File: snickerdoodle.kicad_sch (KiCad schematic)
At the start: 8 parts, among them P2 TFM-115-01-F-D-A, P3 TFM-120-01-F-D-A

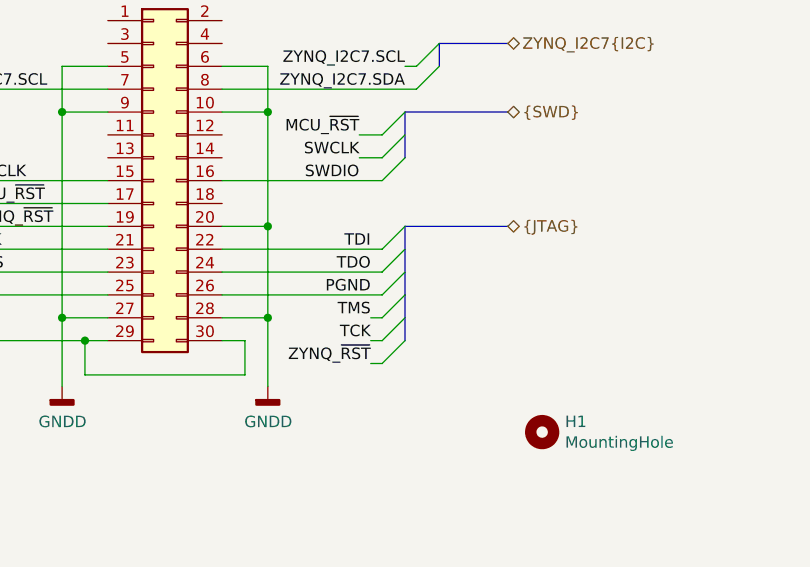
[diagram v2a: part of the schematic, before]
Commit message: Working on gigabit ethernet PHY
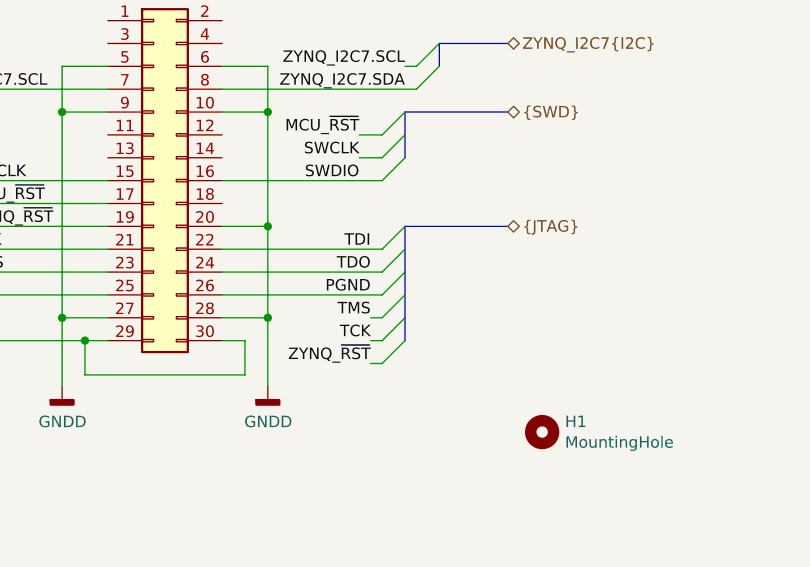
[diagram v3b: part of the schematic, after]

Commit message: Annotate schematic
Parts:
- renumbered H1 to H401, P2 to P401, P3 to P402, PA1 to PA401, PA2 to PA402, PB1 to PB401, PB2 to PB402, PC1 to PC401
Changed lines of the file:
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@@
-(kicad_sch (version 20200618) (host eeschema "5.99.0-unknown-1463dd1~101~ubuntu20.04.1")
-  (page 4 13)
-  (paper "A4")
+(kicad_sch (version 20200618) (host eeschema "5.99.0-unknown-77313e4~101~ubuntu20.04.1")
+  (page 1 13)
+  (paper "B")
   (title_block
     (title "Snickerdoodle Interconnect")
@@
     (comment 1 "Drawn by: Cameron McQuinn")
   )
+  (bus_alias "INTERRUPT" (members "~INT1" "~INT2"))
+  (bus_alias "I2C" (members "SDA" "SCL"))
+  (bus_alias "JTAG" (members "TDI" "TDO" "TCK" "TMS" "ZYNQ_~RST" "PGND"))
   (bus_alias "SWD" (members "MCU_~RST" "SWCLK" "SWDIO"))
-  (bus_alias "JTAG" (members "TDI" "TDO" "TCK" "TMS" "ZYNQ_~RST" "PGND"))
-  (bus_alias "I2C" (members "SDA" "SCL"))
-  (bus_alias "INTERRUPT" (members "~INT1" "~INT2"))
   (junction (at 40.64 45.72) (diameter 0) (color 0 0 0 0))
   (junction (at 40.64 53.34) (diameter 0) (color 0 0 0 0))
@@
   (symbol (lib_id "Snickerdoodle:3.3V_VIO") (at 182.88 134.62 0) (unit 1)
     (in_bom yes) (on_board yes)
-    (property "Reference" "#PWR0115" (id 0) (at 182.88 138.43 0)
+    (property "Reference" "#PWR0410" (id 0) (at 182.88 138.43 0)
       (effects (font (size 1.27 1.27)) hide)
     )
@@
   (symbol (lib_id "power:GNDD") (at 40.64 83.82 0) (mirror y) (unit 1)
     (in_bom yes) (on_board yes)
-    (property "Reference" "#PWR0106" (id 0) (at 40.64 90.17 0)
+    (property "Reference" "#PWR0401" (id 0) (at 40.64 90.17 0)
       (effects (font (size 1.27 1.27)) hide)
     )
@@
   (symbol (lib_id "power:GNDD") (at 40.64 185.42 0) (mirror y) (unit 1)
     (in_bom yes) (on_board yes)
-    (property "Reference" "#PWR0108" (id 0) (at 40.64 191.77 0)
+    (property "Reference" "#PWR0402" (id 0) (at 40.64 191.77 0)
       (effects (font (size 1.27 1.27)) hide)
     )
@@
   (symbol (lib_id "power:GNDD") (at 63.5 83.82 0) (unit 1)
     (in_bom yes) (on_board yes)
-    (property "Reference" "#PWR0104" (id 0) (at 63.5 90.17 0)
+    (property "Reference" "#PWR0403" (id 0) (at 63.5 90.17 0)
       (effects (font (size 1.27 1.27)) hide)
     )
@@
   (symbol (lib_id "power:GNDD") (at 63.5 185.42 0) (unit 1)
     (in_bom yes) (on_board yes)
-    (property "Reference" "#PWR0107" (id 0) (at 63.5 191.77 0)
+    (property "Reference" "#PWR0404" (id 0) (at 63.5 191.77 0)
       (effects (font (size 1.27 1.27)) hide)
     )
@@
   (symbol (lib_id "power:GNDD") (at 104.14 83.82 0) (mirror y) (unit 1)
     (in_bom yes) (on_board yes)
-    (property "Reference" "#PWR0105" (id 0) (at 104.14 90.17 0)
+    (property "Reference" "#PWR0405" (id 0) (at 104.14 90.17 0)
       (effects (font (size 1.27 1.27)) hide)
     )
@@
   (symbol (lib_id "power:GNDD") (at 104.14 185.42 0) (mirror y) (unit 1)
     (in_bom yes) (on_board yes)
-    (property "Reference" "#PWR0101" (id 0) (at 104.14 191.77 0)
+    (property "Reference" "#PWR0406" (id 0) (at 104.14 191.77 0)
       (effects (font (size 1.27 1.27)) hide)
     )
@@
   (symbol (lib_id "power:GNDD") (at 127 83.82 0) (unit 1)
     (in_bom yes) (on_board yes)
-    (property "Reference" "#PWR0103" (id 0) (at 127 90.17 0)
+    (property "Reference" "#PWR0407" (id 0) (at 127 90.17 0)
       (effects (font (size 1.27 1.27)) hide)
     )
@@
   (symbol (lib_id "power:GNDD") (at 127 185.42 0) (unit 1)
     (in_bom yes) (on_board yes)
-    (property "Reference" "#PWR0102" (id 0) (at 127 191.77 0)
+    (property "Reference" "#PWR0408" (id 0) (at 127 191.77 0)
       (effects (font (size 1.27 1.27)) hide)
     )
@@
   (symbol (lib_id "power:GNDD") (at 167.64 83.82 0) (mirror y) (unit 1)
     (in_bom yes) (on_board yes)
-    (property "Reference" "#PWR0113" (id 0) (at 167.64 90.17 0)
+    (property "Reference" "#PWR0409" (id 0) (at 167.64 90.17 0)
       (effects (font (size 1.27 1.27)) hide)
     )
@@
   (symbol (lib_id "power:GNDD") (at 190.5 83.82 0) (unit 1)
     (in_bom yes) (on_board yes)
-    (property "Reference" "#PWR0114" (id 0) (at 190.5 90.17 0)
+    (property "Reference" "#PWR0411" (id 0) (at 190.5 90.17 0)
       (effects (font (size 1.27 1.27)) hide)
     )
@@
   (symbol (lib_id "power:GNDD") (at 200.66 147.32 0) (unit 1)
     (in_bom yes) (on_board yes)
-    (property "Reference" "#PWR0109" (id 0) (at 200.66 153.67 0)
+    (property "Reference" "#PWR0412" (id 0) (at 200.66 153.67 0)
       (effects (font (size 1.27 1.27)) hide)
     )
@@
   (symbol (lib_id "power:GNDD") (at 223.52 147.32 0) (unit 1)
     (in_bom yes) (on_board yes)
-    (property "Reference" "#PWR0112" (id 0) (at 223.52 153.67 0)
+    (property "Reference" "#PWR0413" (id 0) (at 223.52 153.67 0)
       (effects (font (size 1.27 1.27)) hide)
     )
@@
   (symbol (lib_id "power:GNDD") (at 231.14 83.82 0) (mirror y) (unit 1)
     (in_bom yes) (on_board yes)
-    (property "Reference" "#PWR0110" (id 0) (at 231.14 90.17 0)
+    (property "Reference" "#PWR0414" (id 0) (at 231.14 90.17 0)
       (effects (font (size 1.27 1.27)) hide)
     )
@@
   (symbol (lib_id "power:GNDD") (at 254 83.82 0) (unit 1)
     (in_bom yes) (on_board yes)
-    (property "Reference" "#PWR0111" (id 0) (at 254 90.17 0)
+    (property "Reference" "#PWR0415" (id 0) (at 254 90.17 0)
       (effects (font (size 1.27 1.27)) hide)
     )
@@
   (symbol (lib_id "Mechanical:MountingHole") (at 254 152.4 0) (unit 1)
     (in_bom yes) (on_board yes)
-    (property "Reference" "H1" (id 0) (at 256.5401 151.2506 0)
+    (property "Reference" "H401" (id 0) (at 256.5401 151.2506 0)
       (effects (font (size 1.27 1.27)) (justify left))
     )
@@
   (symbol (lib_id "Connector_Generic:Conn_02x15_Odd_Even") (at 210.82 124.46 0) (unit 1)
     (in_bom yes) (on_board yes)
-    (property "Reference" "P2" (id 0) (at 212.09 101.1998 0))
+    (property "Reference" "P401" (id 0) (at 212.09 101.1998 0))
     (property "Value" "TFM-115-01-F-D-A" (id 1) (at 212.09 103.4985 0))
     (property "Footprint" "Connector_Samtec_TFM:Samtec_TFM-115-01-F-D-A_2x15_P1.27mm_Horizontal" (id 2) (at 210.82 124.46 0)
@@
   (symbol (lib_id "Connector_Generic:Conn_02x20_Odd_Even") (at 50.8 50.8 0) (unit 1)
     (in_bom yes) (on_board yes)
-    (property "Reference" "PA1" (id 0) (at 52.07 22.46 0))
+    (property "Reference" "PA401" (id 0) (at 52.07 22.46 0))
     (property "Value" "TFM-120-01-F-D-A" (id 1) (at 52.07 24.7585 0))
     (property "Footprint" "Connector_Samtec_TFM:Samtec_TFM-120-01-F-D-A_2x20_P1.27mm_Horizontal" (id 2) (at 50.8 50.8 0)
@@
   (symbol (lib_id "Connector_Generic:Conn_02x20_Odd_Even") (at 50.8 152.4 0) (unit 1)
     (in_bom yes) (on_board yes)
-    (property "Reference" "PB1" (id 0) (at 52.07 124.06 0))
+    (property "Reference" "PB401" (id 0) (at 52.07 124.06 0))
     (property "Value" "TFM-120-01-F-D-A" (id 1) (at 52.07 126.3585 0))
     (property "Footprint" "Connector_Samtec_TFM:Samtec_TFM-120-01-F-D-A_2x20_P1.27mm_Horizontal" (id 2) (at 50.8 152.4 0)
@@
   (symbol (lib_id "Connector_Generic:Conn_02x20_Odd_Even") (at 114.3 50.8 0) (unit 1)
     (in_bom yes) (on_board yes)
-    (property "Reference" "PA2" (id 0) (at 115.57 22.46 0))
+    (property "Reference" "PA402" (id 0) (at 115.57 22.46 0))
     (property "Value" "TFM-120-01-F-D-A" (id 1) (at 115.57 24.7585 0))
     (property "Footprint" "Connector_Samtec_TFM:Samtec_TFM-120-01-F-D-A_2x20_P1.27mm_Horizontal" (id 2) (at 114.3 50.8 0)
@@
   (symbol (lib_id "Connector_Generic:Conn_02x20_Odd_Even") (at 114.3 152.4 0) (unit 1)
     (in_bom yes) (on_board yes)
-    (property "Reference" "PB2" (id 0) (at 115.57 124.06 0))
+    (property "Reference" "PB402" (id 0) (at 115.57 124.06 0))
     (property "Value" "TFM-120-01-F-D-A" (id 1) (at 115.57 126.3585 0))
     (property "Footprint" "Connector_Samtec_TFM:Samtec_TFM-120-01-F-D-A_2x20_P1.27mm_Horizontal" (id 2) (at 114.3 152.4 0)
@@
   (symbol (lib_id "Connector_Generic:Conn_02x20_Odd_Even") (at 177.8 50.8 0) (unit 1)
     (in_bom yes) (on_board yes)
-    (property "Reference" "PC1" (id 0) (at 179.07 22.46 0))
+    (property "Reference" "PC401" (id 0) (at 179.07 22.46 0))
     (property "Value" "TFM-120-01-F-D-A" (id 1) (at 179.07 24.7585 0))
     (property "Footprint" "Connector_Samtec_TFM:Samtec_TFM-120-01-F-D-A_2x20_P1.27mm_Horizontal" (id 2) (at 177.8 50.8 0)
@@
   (symbol (lib_id "Connector_Generic:Conn_02x20_Odd_Even") (at 241.3 50.8 0) (unit 1)
     (in_bom yes) (on_board yes)
-    (property "Reference" "P3" (id 0) (at 242.57 22.46 0))
+    (property "Reference" "P402" (id 0) (at 242.57 22.46 0))
     (property "Value" "TFM-120-01-F-D-A" (id 1) (at 242.57 24.7585 0))
     (property "Footprint" "Connector_Samtec_TFM:Samtec_TFM-120-01-F-D-A_2x20_P1.27mm_Horizontal" (id 2) (at 241.3 50.8 0)

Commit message: Fix footprint associations, use 74LVC2G07 instead of MOSFETs
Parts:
- renumbered H401 to H501, P401 to P501, P402 to P502, PA401 to PA501, PA402 to PA502, PB401 to PB501, PB402 to PB502, PC401 to PC501
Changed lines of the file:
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@@
     (comment 1 "Drawn by: Cameron McQuinn")
   )
-  (bus_alias "INTERRUPT" (members "~INT1" "~INT2"))
+  (bus_alias "SWD" (members "MCU_~RST" "SWCLK" "SWDIO"))
   (bus_alias "I2C" (members "SDA" "SCL"))
   (bus_alias "JTAG" (members "TDI" "TDO" "TCK" "TMS" "ZYNQ_~RST" "PGND"))
-  (bus_alias "SWD" (members "MCU_~RST" "SWCLK" "SWDIO"))
+  (bus_alias "INTERRUPT" (members "~INT1" "~INT2"))
   (junction (at 40.64 45.72) (diameter 0) (color 0 0 0 0))
   (junction (at 40.64 53.34) (diameter 0) (color 0 0 0 0))
@@
   (symbol (lib_id "Snickerdoodle:3.3V_VIO") (at 182.88 134.62 0) (unit 1)
     (in_bom yes) (on_board yes)
-    (property "Reference" "#PWR0410" (id 0) (at 182.88 138.43 0)
+    (property "Reference" "#PWR0510" (id 0) (at 182.88 138.43 0)
       (effects (font (size 1.27 1.27)) hide)
     )
@@
   (symbol (lib_id "power:GNDD") (at 40.64 83.82 0) (mirror y) (unit 1)
     (in_bom yes) (on_board yes)
-    (property "Reference" "#PWR0401" (id 0) (at 40.64 90.17 0)
+    (property "Reference" "#PWR0501" (id 0) (at 40.64 90.17 0)
       (effects (font (size 1.27 1.27)) hide)
     )
@@
   (symbol (lib_id "power:GNDD") (at 40.64 185.42 0) (mirror y) (unit 1)
     (in_bom yes) (on_board yes)
-    (property "Reference" "#PWR0402" (id 0) (at 40.64 191.77 0)
+    (property "Reference" "#PWR0502" (id 0) (at 40.64 191.77 0)
       (effects (font (size 1.27 1.27)) hide)
     )
@@
   (symbol (lib_id "power:GNDD") (at 63.5 83.82 0) (unit 1)
     (in_bom yes) (on_board yes)
-    (property "Reference" "#PWR0403" (id 0) (at 63.5 90.17 0)
+    (property "Reference" "#PWR0503" (id 0) (at 63.5 90.17 0)
       (effects (font (size 1.27 1.27)) hide)
     )
@@
   (symbol (lib_id "power:GNDD") (at 63.5 185.42 0) (unit 1)
     (in_bom yes) (on_board yes)
-    (property "Reference" "#PWR0404" (id 0) (at 63.5 191.77 0)
+    (property "Reference" "#PWR0504" (id 0) (at 63.5 191.77 0)
       (effects (font (size 1.27 1.27)) hide)
     )
@@
   (symbol (lib_id "power:GNDD") (at 104.14 83.82 0) (mirror y) (unit 1)
     (in_bom yes) (on_board yes)
-    (property "Reference" "#PWR0405" (id 0) (at 104.14 90.17 0)
+    (property "Reference" "#PWR0505" (id 0) (at 104.14 90.17 0)
       (effects (font (size 1.27 1.27)) hide)
     )
@@
   (symbol (lib_id "power:GNDD") (at 104.14 185.42 0) (mirror y) (unit 1)
     (in_bom yes) (on_board yes)
-    (property "Reference" "#PWR0406" (id 0) (at 104.14 191.77 0)
+    (property "Reference" "#PWR0506" (id 0) (at 104.14 191.77 0)
       (effects (font (size 1.27 1.27)) hide)
     )
@@
   (symbol (lib_id "power:GNDD") (at 127 83.82 0) (unit 1)
     (in_bom yes) (on_board yes)
-    (property "Reference" "#PWR0407" (id 0) (at 127 90.17 0)
+    (property "Reference" "#PWR0507" (id 0) (at 127 90.17 0)
       (effects (font (size 1.27 1.27)) hide)
     )
@@
   (symbol (lib_id "power:GNDD") (at 127 185.42 0) (unit 1)
     (in_bom yes) (on_board yes)
-    (property "Reference" "#PWR0408" (id 0) (at 127 191.77 0)
+    (property "Reference" "#PWR0508" (id 0) (at 127 191.77 0)
       (effects (font (size 1.27 1.27)) hide)
     )
@@
   (symbol (lib_id "power:GNDD") (at 167.64 83.82 0) (mirror y) (unit 1)
     (in_bom yes) (on_board yes)
-    (property "Reference" "#PWR0409" (id 0) (at 167.64 90.17 0)
+    (property "Reference" "#PWR0509" (id 0) (at 167.64 90.17 0)
       (effects (font (size 1.27 1.27)) hide)
     )
@@
   (symbol (lib_id "power:GNDD") (at 190.5 83.82 0) (unit 1)
     (in_bom yes) (on_board yes)
-    (property "Reference" "#PWR0411" (id 0) (at 190.5 90.17 0)
+    (property "Reference" "#PWR0511" (id 0) (at 190.5 90.17 0)
       (effects (font (size 1.27 1.27)) hide)
     )
@@
   (symbol (lib_id "power:GNDD") (at 200.66 147.32 0) (unit 1)
     (in_bom yes) (on_board yes)
-    (property "Reference" "#PWR0412" (id 0) (at 200.66 153.67 0)
+    (property "Reference" "#PWR0512" (id 0) (at 200.66 153.67 0)
       (effects (font (size 1.27 1.27)) hide)
     )
@@
   (symbol (lib_id "power:GNDD") (at 223.52 147.32 0) (unit 1)
     (in_bom yes) (on_board yes)
-    (property "Reference" "#PWR0413" (id 0) (at 223.52 153.67 0)
+    (property "Reference" "#PWR0513" (id 0) (at 223.52 153.67 0)
       (effects (font (size 1.27 1.27)) hide)
     )
@@
   (symbol (lib_id "power:GNDD") (at 231.14 83.82 0) (mirror y) (unit 1)
     (in_bom yes) (on_board yes)
-    (property "Reference" "#PWR0414" (id 0) (at 231.14 90.17 0)
+    (property "Reference" "#PWR0514" (id 0) (at 231.14 90.17 0)
       (effects (font (size 1.27 1.27)) hide)
     )
@@
   (symbol (lib_id "power:GNDD") (at 254 83.82 0) (unit 1)
     (in_bom yes) (on_board yes)
-    (property "Reference" "#PWR0415" (id 0) (at 254 90.17 0)
+    (property "Reference" "#PWR0515" (id 0) (at 254 90.17 0)
       (effects (font (size 1.27 1.27)) hide)
     )
@@
   (symbol (lib_id "Mechanical:MountingHole") (at 254 152.4 0) (unit 1)
     (in_bom yes) (on_board yes)
-    (property "Reference" "H401" (id 0) (at 256.5401 151.2506 0)
+    (property "Reference" "H501" (id 0) (at 256.5401 151.2506 0)
       (effects (font (size 1.27 1.27)) (justify left))
     )
@@
   (symbol (lib_id "Connector_Generic:Conn_02x15_Odd_Even") (at 210.82 124.46 0) (unit 1)
     (in_bom yes) (on_board yes)
-    (property "Reference" "P401" (id 0) (at 212.09 101.1998 0))
+    (property "Reference" "P501" (id 0) (at 212.09 101.1998 0))
     (property "Value" "TFM-115-01-F-D-A" (id 1) (at 212.09 103.4985 0))
     (property "Footprint" "Connector_Samtec_TFM:Samtec_TFM-115-01-F-D-A_2x15_P1.27mm_Horizontal" (id 2) (at 210.82 124.46 0)
@@
   (symbol (lib_id "Connector_Generic:Conn_02x20_Odd_Even") (at 50.8 50.8 0) (unit 1)
     (in_bom yes) (on_board yes)
-    (property "Reference" "PA401" (id 0) (at 52.07 22.46 0))
+    (property "Reference" "PA501" (id 0) (at 52.07 22.46 0))
     (property "Value" "TFM-120-01-F-D-A" (id 1) (at 52.07 24.7585 0))
     (property "Footprint" "Connector_Samtec_TFM:Samtec_TFM-120-01-F-D-A_2x20_P1.27mm_Horizontal" (id 2) (at 50.8 50.8 0)
@@
   (symbol (lib_id "Connector_Generic:Conn_02x20_Odd_Even") (at 50.8 152.4 0) (unit 1)
     (in_bom yes) (on_board yes)
-    (property "Reference" "PB401" (id 0) (at 52.07 124.06 0))
+    (property "Reference" "PB501" (id 0) (at 52.07 124.06 0))
     (property "Value" "TFM-120-01-F-D-A" (id 1) (at 52.07 126.3585 0))
     (property "Footprint" "Connector_Samtec_TFM:Samtec_TFM-120-01-F-D-A_2x20_P1.27mm_Horizontal" (id 2) (at 50.8 152.4 0)
@@
   (symbol (lib_id "Connector_Generic:Conn_02x20_Odd_Even") (at 114.3 50.8 0) (unit 1)
     (in_bom yes) (on_board yes)
-    (property "Reference" "PA402" (id 0) (at 115.57 22.46 0))
+    (property "Reference" "PA502" (id 0) (at 115.57 22.46 0))
     (property "Value" "TFM-120-01-F-D-A" (id 1) (at 115.57 24.7585 0))
     (property "Footprint" "Connector_Samtec_TFM:Samtec_TFM-120-01-F-D-A_2x20_P1.27mm_Horizontal" (id 2) (at 114.3 50.8 0)
@@
   (symbol (lib_id "Connector_Generic:Conn_02x20_Odd_Even") (at 114.3 152.4 0) (unit 1)
     (in_bom yes) (on_board yes)
-    (property "Reference" "PB402" (id 0) (at 115.57 124.06 0))
+    (property "Reference" "PB502" (id 0) (at 115.57 124.06 0))
     (property "Value" "TFM-120-01-F-D-A" (id 1) (at 115.57 126.3585 0))
     (property "Footprint" "Connector_Samtec_TFM:Samtec_TFM-120-01-F-D-A_2x20_P1.27mm_Horizontal" (id 2) (at 114.3 152.4 0)
@@
   (symbol (lib_id "Connector_Generic:Conn_02x20_Odd_Even") (at 177.8 50.8 0) (unit 1)
     (in_bom yes) (on_board yes)
-    (property "Reference" "PC401" (id 0) (at 179.07 22.46 0))
+    (property "Reference" "PC501" (id 0) (at 179.07 22.46 0))
     (property "Value" "TFM-120-01-F-D-A" (id 1) (at 179.07 24.7585 0))
     (property "Footprint" "Connector_Samtec_TFM:Samtec_TFM-120-01-F-D-A_2x20_P1.27mm_Horizontal" (id 2) (at 177.8 50.8 0)
@@
   (symbol (lib_id "Connector_Generic:Conn_02x20_Odd_Even") (at 241.3 50.8 0) (unit 1)
     (in_bom yes) (on_board yes)
-    (property "Reference" "P402" (id 0) (at 242.57 22.46 0))
+    (property "Reference" "P502" (id 0) (at 242.57 22.46 0))
     (property "Value" "TFM-120-01-F-D-A" (id 1) (at 242.57 24.7585 0))
     (property "Footprint" "Connector_Samtec_TFM:Samtec_TFM-120-01-F-D-A_2x20_P1.27mm_Horizontal" (id 2) (at 241.3 50.8 0)

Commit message: Connect Ethernet and USB to MIO, start layout
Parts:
- renumbered P501 to P2, P502 to P3, PA501 to PA1, PA502 to PA2, PB501 to PB1, PB502 to PB2, PC501 to PC1
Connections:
- net ETHERNET.MDC: now reaches PA2.36 (Pin_36)
- net ETHERNET.MDIO: now reaches PA2.38 (Pin_38)
- net ETHERNET.TXD3: now reaches P3.11 (Pin_11)
- net ETHERNET.RXD0: now reaches P3.12 (Pin_12)
- net ETHERNET.TX_CTL: now reaches P3.13 (Pin_13)
- net ETHERNET.RX_CLK: now reaches P3.14 (Pin_14)
- net ETHERNET.RXD1: now reaches P3.17 (Pin_17)
- net ETHERNET.RX_CTL: now reaches P3.18 (Pin_18)
- net ETHERNET.RXD2: now reaches P3.19 (Pin_19)
- net ~ETHERNET_RST: now reaches P3.2 (Pin_2)
- net ETHERNET.RXD3: now reaches P3.20 (Pin_20)
- net USB.DATA4: now reaches P3.23 (Pin_23)
- net USB.NXT: now reaches P3.24 (Pin_24)
- net USB.DIR: now reaches P3.25 (Pin_25)
- net USB.STP: now reaches P3.26 (Pin_26)
- net USB.DATA0: now reaches P3.29 (Pin_29)
- net USB.DATA3: now reaches P3.30 (Pin_30)
- net USB.DATA1: now reaches P3.31 (Pin_31)
- net USB.DATA2: now reaches P3.32 (Pin_32)
- net USB.CLK: now reaches P3.35 (Pin_35)
- net USB.DATA7: now reaches P3.36 (Pin_36)
- net USB.DATA5: now reaches P3.37 (Pin_37)
- net USB.DATA6: now reaches P3.38 (Pin_38)
- net ~USB_RST: now reaches P3.4 (Pin_4)
- net ETHERNET.TX_CLK: now reaches P3.5 (Pin_5)
- net ETHERNET.TXD2: now reaches P3.6 (Pin_6)
- net ETHERNET.TXD0: now reaches P3.7 (Pin_7)
- net ETHERNET.TXD1: now reaches P3.8 (Pin_8)
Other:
- moved on the sheet: H501, P2, P3, PA1, PA2, PB1, PB2, PC1
